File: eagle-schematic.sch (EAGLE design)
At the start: 30 parts, among them IC1 74HC595N, IC2 74HC595N, IC3 74HC595N, IC4 74HC595N, J1 DCJ0202, M1 DC-DC_5-15V_TO_5V

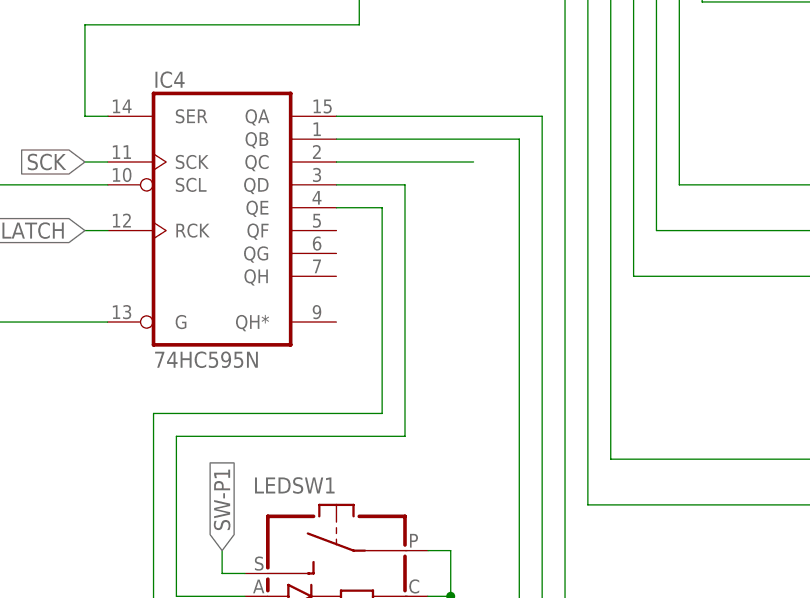
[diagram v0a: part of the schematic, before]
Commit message: Changed wrong connection in schematic
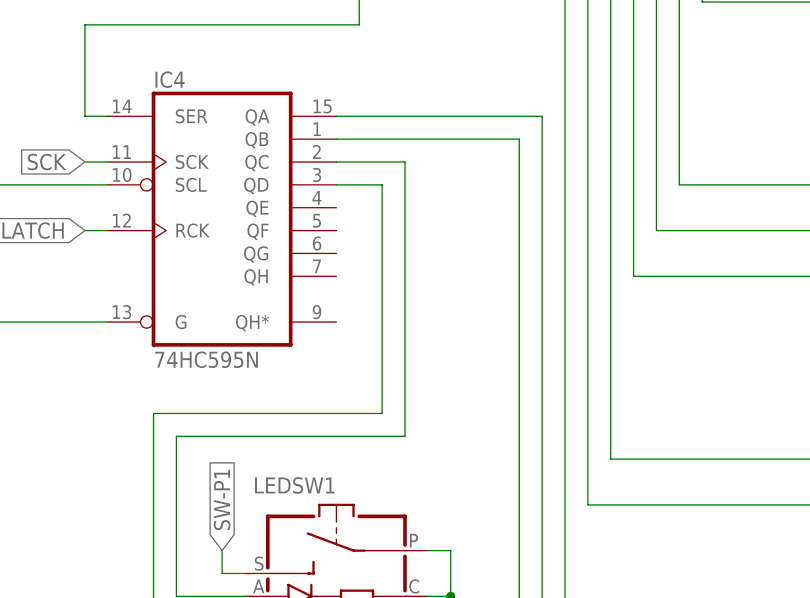
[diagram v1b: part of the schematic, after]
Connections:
- removed net N$39: IC4A.QC
- net N$40: now also IC4A.QC; no longer IC4A.QD
- net N$41: now also IC4A.QD; no longer IC4A.QE
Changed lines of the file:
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@@
-</segment>
-</net>
-<net name="N$39" class="0">
-<segment>
-<pinref part="IC4" gate="A" pin="QC"/>
-<wire x1="210.82" y1="35.56" x2="226.06" y2="35.56" width="0.1524" layer="91"/>
 </segment>
 </net>
@@
 <wire x1="193.04" y1="-12.7" x2="193.04" y2="5.08" width="0.1524" layer="91"/>
 <wire x1="193.04" y1="5.08" x2="218.44" y2="5.08" width="0.1524" layer="91"/>
-<pinref part="IC4" gate="A" pin="QD"/>
-<wire x1="218.44" y1="5.08" x2="218.44" y2="33.02" width="0.1524" layer="91"/>
-<wire x1="218.44" y1="33.02" x2="210.82" y2="33.02" width="0.1524" layer="91"/>
+<wire x1="218.44" y1="5.08" x2="218.44" y2="35.56" width="0.1524" layer="91"/>
 <pinref part="LEDSW1" gate="G$1" pin="A"/>
 <wire x1="200.66" y1="-12.7" x2="193.04" y2="-12.7" width="0.1524" layer="91"/>
+<pinref part="IC4" gate="A" pin="QC"/>
+<wire x1="210.82" y1="35.56" x2="218.44" y2="35.56" width="0.1524" layer="91"/>
 </segment>
 </net>
 <net name="N$41" class="0">
 <segment>
-<pinref part="IC4" gate="A" pin="QE"/>
-<wire x1="210.82" y1="30.48" x2="215.9" y2="30.48" width="0.1524" layer="91"/>
-<wire x1="215.9" y1="30.48" x2="215.9" y2="7.62" width="0.1524" layer="91"/>
+<wire x1="215.9" y1="33.02" x2="215.9" y2="7.62" width="0.1524" layer="91"/>
 <wire x1="215.9" y1="7.62" x2="190.5" y2="7.62" width="0.1524" layer="91"/>
 <wire x1="190.5" y1="7.62" x2="190.5" y2="-40.64" width="0.1524" layer="91"/>
 <pinref part="LEDSW2" gate="G$1" pin="A"/>
 <wire x1="200.66" y1="-40.64" x2="190.5" y2="-40.64" width="0.1524" layer="91"/>
+<pinref part="IC4" gate="A" pin="QD"/>
+<wire x1="210.82" y1="33.02" x2="215.9" y2="33.02" width="0.1524" layer="91"/>
 </segment>
 </net>

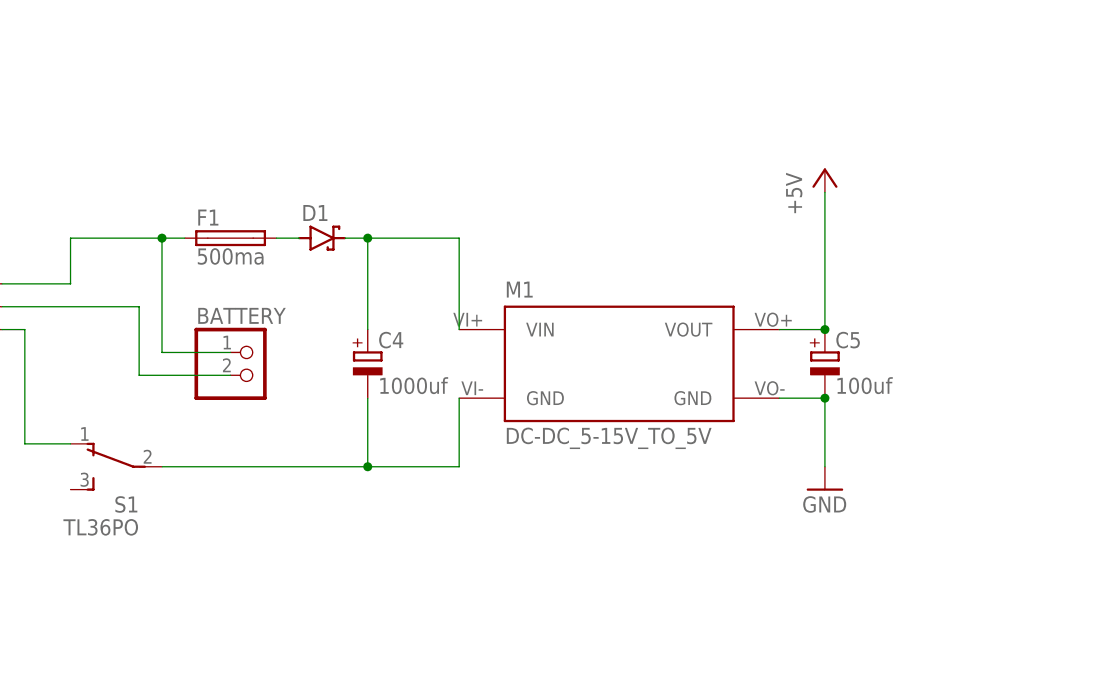
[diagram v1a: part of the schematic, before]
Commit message: Added missing diode value
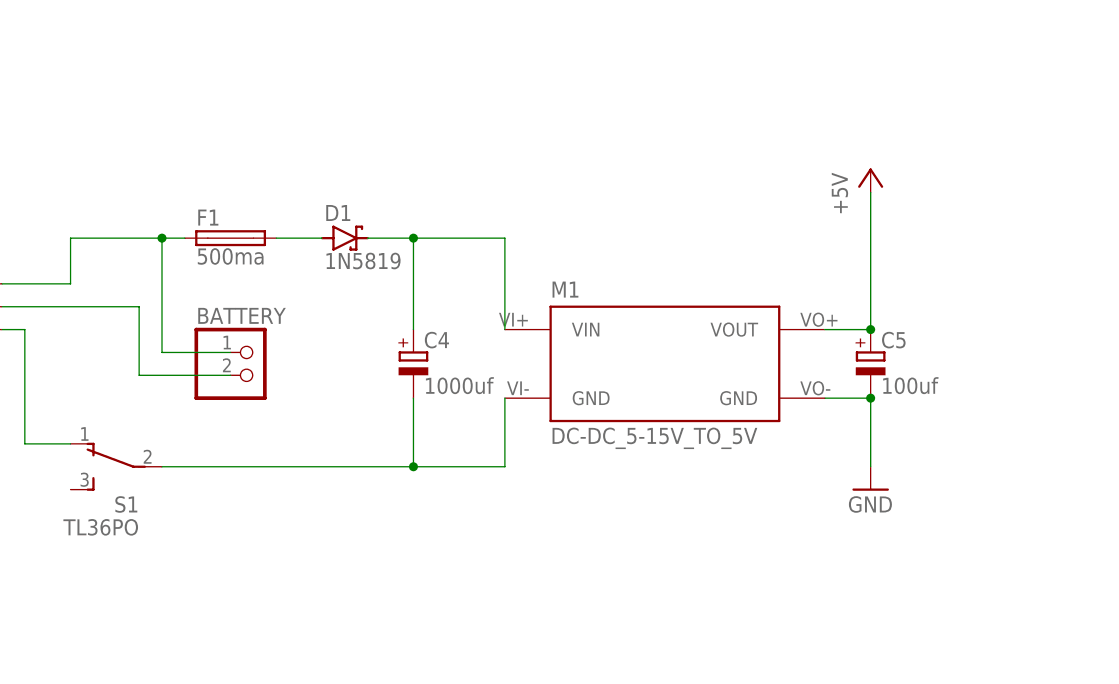
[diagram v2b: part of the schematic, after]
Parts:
- D1: value (none) -> 1N5819
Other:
- moved on the sheet: C4, C5, D1, M1
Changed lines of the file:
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@@
 <part name="F1" library="fuse" library_urn="urn:adsk.eagle:library:233" deviceset="FUSE" device="BLANK_5X20MM" package3d_urn="urn:adsk.eagle:package:14079/1" value="500ma"/>
 <part name="P+1" library="supply1" library_urn="urn:adsk.eagle:library:371" deviceset="+5V" device=""/>
-<part name="D1" library="diode" library_urn="urn:adsk.eagle:library:210" deviceset="SCHOTTKY-DIODE" device="CB417-15" package3d_urn="urn:adsk.eagle:package:43349/2"/>
+<part name="D1" library="diode" library_urn="urn:adsk.eagle:library:210" deviceset="SCHOTTKY-DIODE" device="CB417-15" package3d_urn="urn:adsk.eagle:package:43349/2" value="1N5819"/>
 <part name="R1" library="pot" library_urn="urn:adsk.eagle:library:331" deviceset="TRIM_EU-" device="CIP20C-4MM" package3d_urn="urn:adsk.eagle:package:22718/1" value="10K"/>
 <part name="GND3" library="supply1" library_urn="urn:adsk.eagle:library:371" deviceset="GND" device=""/>
@@
 <attribute name="VALUE" x="116.84" y="81.28" size="1.778" layer="96" rot="R90"/>
 </instance>
-<instance part="D1" gate="G$1" x="66.04" y="144.78" smashed="yes">
-<attribute name="NAME" x="63.754" y="146.685" size="1.778" layer="95"/>
-<attribute name="VALUE" x="63.754" y="141.351" size="1.778" layer="96"/>
+<instance part="D1" gate="G$1" x="68.58" y="144.78" smashed="yes">
+<attribute name="NAME" x="66.294" y="146.685" size="1.778" layer="95"/>
+<attribute name="VALUE" x="66.294" y="141.351" size="1.778" layer="96"/>
 </instance>
 <instance part="R1" gate="1" x="127" y="66.04" smashed="yes" rot="MR0">
@@
 <attribute name="VALUE" x="134.62" y="53.34" size="1.778" layer="96"/>
 </instance>
-<instance part="C4" gate="G$1" x="71.12" y="132.08" smashed="yes">
-<attribute name="NAME" x="72.263" y="132.5626" size="1.778" layer="95"/>
-<attribute name="VALUE" x="72.263" y="127.4826" size="1.778" layer="96"/>
-</instance>
-<instance part="C5" gate="G$1" x="121.92" y="132.08" smashed="yes">
-<attribute name="NAME" x="123.063" y="132.5626" size="1.778" layer="95"/>
-<attribute name="VALUE" x="123.063" y="127.4826" size="1.778" layer="96"/>
-</instance>
-<instance part="M1" gate="G$1" x="99.06" y="132.08" smashed="yes">
-<attribute name="NAME" x="86.36" y="138.176" size="1.778" layer="95"/>
-<attribute name="VALUE" x="86.36" y="121.92" size="1.778" layer="96"/>
-</instance>
-<instance part="P+3" gate="1" x="121.92" y="152.4" smashed="yes">
-<attribute name="VALUE" x="119.38" y="147.32" size="1.778" layer="96" rot="R90"/>
-</instance>
-<instance part="GND2" gate="1" x="121.92" y="116.84" smashed="yes">
-<attribute name="VALUE" x="119.38" y="114.3" size="1.778" layer="96"/>
+<instance part="C4" gate="G$1" x="76.2" y="132.08" smashed="yes">
+<attribute name="NAME" x="77.343" y="132.5626" size="1.778" layer="95"/>
+<attribute name="VALUE" x="77.343" y="127.4826" size="1.778" layer="96"/>
+</instance>
+<instance part="C5" gate="G$1" x="127" y="132.08" smashed="yes">
+<attribute name="NAME" x="128.143" y="132.5626" size="1.778" layer="95"/>
+<attribute name="VALUE" x="128.143" y="127.4826" size="1.778" layer="96"/>
+</instance>
+<instance part="M1" gate="G$1" x="104.14" y="132.08" smashed="yes">
+<attribute name="NAME" x="91.44" y="138.176" size="1.778" layer="95"/>
+<attribute name="VALUE" x="91.44" y="121.92" size="1.778" layer="96"/>
+</instance>
+<instance part="P+3" gate="1" x="127" y="152.4" smashed="yes">
+<attribute name="VALUE" x="124.46" y="147.32" size="1.778" layer="96" rot="R90"/>
+</instance>
+<instance part="GND2" gate="1" x="127" y="116.84" smashed="yes">
+<attribute name="VALUE" x="124.46" y="114.3" size="1.778" layer="96"/>
 </instance>
 <instance part="BATTERY" gate="G$1" x="58.42" y="129.54" smashed="yes">
@@
 <pinref part="M1" gate="G$1" pin="GND@2"/>
 <pinref part="C5" gate="G$1" pin="-"/>
-<wire x1="116.84" y1="127" x2="121.92" y2="127" width="0.1524" layer="91"/>
+<wire x1="121.92" y1="127" x2="127" y2="127" width="0.1524" layer="91"/>
 <pinref part="GND2" gate="1" pin="GND"/>
-<wire x1="121.92" y1="119.38" x2="121.92" y2="127" width="0.1524" layer="91"/>
-<junction x="121.92" y="127"/>
+<wire x1="127" y1="119.38" x2="127" y2="127" width="0.1524" layer="91"/>
+<junction x="127" y="127"/>
 </segment>
 <segment>
@@
 <pinref part="M1" gate="G$1" pin="VOUT"/>
 <pinref part="C5" gate="G$1" pin="+"/>
-<wire x1="116.84" y1="134.62" x2="121.92" y2="134.62" width="0.1524" layer="91"/>
+<wire x1="121.92" y1="134.62" x2="127" y2="134.62" width="0.1524" layer="91"/>
 <pinref part="P+3" gate="1" pin="+5V"/>
-<wire x1="121.92" y1="149.86" x2="121.92" y2="134.62" width="0.1524" layer="91"/>
-<junction x="121.92" y="134.62"/>
+<wire x1="127" y1="149.86" x2="127" y2="134.62" width="0.1524" layer="91"/>
+<junction x="127" y="134.62"/>
 </segment>
 <segment>
@@
 <pinref part="D1" gate="G$1" pin="A"/>
 <pinref part="F1" gate="G$1" pin="2"/>
-<wire x1="63.5" y1="144.78" x2="60.96" y2="144.78" width="0.1524" layer="91"/>
+<wire x1="66.04" y1="144.78" x2="60.96" y2="144.78" width="0.1524" layer="91"/>
 </segment>
 </net>
@@
 <pinref part="D1" gate="G$1" pin="C"/>
 <pinref part="C4" gate="G$1" pin="+"/>
-<wire x1="68.58" y1="144.78" x2="71.12" y2="144.78" width="0.1524" layer="91"/>
-<wire x1="71.12" y1="144.78" x2="71.12" y2="134.62" width="0.1524" layer="91"/>
+<wire x1="71.12" y1="144.78" x2="76.2" y2="144.78" width="0.1524" layer="91"/>
+<wire x1="76.2" y1="144.78" x2="76.2" y2="134.62" width="0.1524" layer="91"/>
 <pinref part="M1" gate="G$1" pin="VIN"/>
-<wire x1="81.28" y1="134.62" x2="81.28" y2="144.78" width="0.1524" layer="91"/>
-<wire x1="81.28" y1="144.78" x2="71.12" y2="144.78" width="0.1524" layer="91"/>
-<junction x="71.12" y="144.78"/>
+<wire x1="86.36" y1="134.62" x2="86.36" y2="144.78" width="0.1524" layer="91"/>
+<wire x1="86.36" y1="144.78" x2="76.2" y2="144.78" width="0.1524" layer="91"/>
+<junction x="76.2" y="144.78"/>
 </segment>
 </net>
@@
 <pinref part="S1" gate="BEF1" pin="P"/>
 <pinref part="C4" gate="G$1" pin="-"/>
-<wire x1="71.12" y1="127" x2="71.12" y2="119.38" width="0.1524" layer="91"/>
-<wire x1="71.12" y1="119.38" x2="48.26" y2="119.38" width="0.1524" layer="91"/>
+<wire x1="76.2" y1="127" x2="76.2" y2="119.38" width="0.1524" layer="91"/>
+<wire x1="76.2" y1="119.38" x2="48.26" y2="119.38" width="0.1524" layer="91"/>
 <pinref part="M1" gate="G$1" pin="GND@1"/>
-<wire x1="81.28" y1="127" x2="81.28" y2="119.38" width="0.1524" layer="91"/>
-<wire x1="81.28" y1="119.38" x2="71.12" y2="119.38" width="0.1524" layer="91"/>
-<junction x="71.12" y="119.38"/>
-</segment>
-</net>
+<wire x1="86.36" y1="127" x2="86.36" y2="119.38" width="0.1524" layer="91"/>
+<wire x1="86.36" y1="119.38" x2="76.2" y2="119.38" width="0.1524" layer="91"/>
+<junction x="76.2" y="119.38"/>
+</segment>
+</net>

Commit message: Updated packages
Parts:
- LEDSW1, LEDSW2: value MCLED -> MC1PLED; device switches-custom:MCLED -> switches-custom:MC1PLED
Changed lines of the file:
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@@
 <part name="P+6" library="supply1" library_urn="urn:adsk.eagle:library:371" deviceset="+5V" device=""/>
 <part name="GND7" library="supply1" library_urn="urn:adsk.eagle:library:371" deviceset="GND" device=""/>
-<part name="RGBSW1" library="switches-custom" deviceset="MC3PRGB" device=""/>
-<part name="RGBSW2" library="switches-custom" deviceset="MC3PRGB" device=""/>
-<part name="RGBSW3" library="switches-custom" deviceset="MC3PRGB" device=""/>
-<part name="RGBSW4" library="switches-custom" deviceset="MC3PRGB" device=""/>
-<part name="RGBSW5" library="switches-custom" deviceset="MC3PRGB" device=""/>
-<part name="RGBSW6" library="switches-custom" deviceset="MC3PRGB" device=""/>
-<part name="RGBSW7" library="switches-custom" deviceset="MC3PRGB" device=""/>
-<part name="RGBSW8" library="switches-custom" deviceset="MC3PRGB" device=""/>
-<part name="RGBSW9" library="switches-custom" deviceset="MC3PRGB" device=""/>
-<part name="LEDSW1" library="switches-custom" library_urn="urn:adsk.eagle:library:37171722" deviceset="MCLED" device="" package3d_urn="urn:adsk.eagle:package:37173483/1"/>
-<part name="LEDSW2" library="switches-custom" library_urn="urn:adsk.eagle:library:37171722" deviceset="MCLED" device="" package3d_urn="urn:adsk.eagle:package:37173483/1"/>
+<part name="RGBSW1" library="switches-custom" library_urn="urn:adsk.eagle:library:37171722" deviceset="MC3PRGB" device="" package3d_urn="urn:adsk.eagle:package:37173484/1"/>
+<part name="RGBSW2" library="switches-custom" library_urn="urn:adsk.eagle:library:37171722" deviceset="MC3PRGB" device="" package3d_urn="urn:adsk.eagle:package:37173484/1"/>
+<part name="RGBSW3" library="switches-custom" library_urn="urn:adsk.eagle:library:37171722" deviceset="MC3PRGB" device="" package3d_urn="urn:adsk.eagle:package:37173484/1"/>
+<part name="RGBSW4" library="switches-custom" library_urn="urn:adsk.eagle:library:37171722" deviceset="MC3PRGB" device="" package3d_urn="urn:adsk.eagle:package:37173484/1"/>
+<part name="RGBSW5" library="switches-custom" library_urn="urn:adsk.eagle:library:37171722" deviceset="MC3PRGB" device="" package3d_urn="urn:adsk.eagle:package:37173484/1"/>
+<part name="RGBSW6" library="switches-custom" library_urn="urn:adsk.eagle:library:37171722" deviceset="MC3PRGB" device="" package3d_urn="urn:adsk.eagle:package:37173484/1"/>
+<part name="RGBSW7" library="switches-custom" library_urn="urn:adsk.eagle:library:37171722" deviceset="MC3PRGB" device="" package3d_urn="urn:adsk.eagle:package:37173484/1"/>
+<part name="RGBSW8" library="switches-custom" library_urn="urn:adsk.eagle:library:37171722" deviceset="MC3PRGB" device="" package3d_urn="urn:adsk.eagle:package:37173484/1"/>
+<part name="RGBSW9" library="switches-custom" library_urn="urn:adsk.eagle:library:37171722" deviceset="MC3PRGB" device="" package3d_urn="urn:adsk.eagle:package:37173484/1"/>
 <part name="GND8" library="supply1" library_urn="urn:adsk.eagle:library:371" deviceset="GND" device=""/>
+<part name="LEDSW1" library="switches-custom" library_urn="urn:adsk.eagle:library:37171722" deviceset="MC1PLED" device="" package3d_urn="urn:adsk.eagle:package:37173483/1"/>
+<part name="LEDSW2" library="switches-custom" library_urn="urn:adsk.eagle:library:37171722" deviceset="MC1PLED" device="" package3d_urn="urn:adsk.eagle:package:37173483/1"/>
 </parts>
 <sheets>
@@
 <attribute name="VALUE" x="294.64" y="-43.18" size="1.778" layer="96" rot="MR0"/>
 </instance>
+<instance part="GND8" gate="1" x="266.7" y="-48.26" smashed="yes">
+<attribute name="VALUE" x="264.16" y="-50.8" size="1.778" layer="96"/>
+</instance>
 <instance part="LEDSW1" gate="G$1" x="210.82" y="-7.62" smashed="yes" rot="MR270">
 <attribute name="NAME" x="210.82" y="-1.27" size="1.778" layer="95" rot="MR0"/>
@@
 <attribute name="NAME" x="210.82" y="-29.21" size="1.778" layer="95" rot="MR0"/>
 <attribute name="VALUE" x="215.9" y="-48.26" size="1.778" layer="96" rot="MR0"/>
-</instance>
-<instance part="GND8" gate="1" x="266.7" y="-48.26" smashed="yes">
-<attribute name="VALUE" x="264.16" y="-50.8" size="1.778" layer="96"/>
 </instance>
 </instances>
@@
 <pinref part="GND8" gate="1" pin="GND"/>
 <junction x="266.7" y="-45.72"/>
-<pinref part="LEDSW1" gate="G$1" pin="P"/>
 <wire x1="220.98" y1="-7.62" x2="223.52" y2="-7.62" width="0.1524" layer="91"/>
-<pinref part="LEDSW1" gate="G$1" pin="C"/>
 <wire x1="220.98" y1="-12.7" x2="223.52" y2="-12.7" width="0.1524" layer="91"/>
 <junction x="223.52" y="-12.7"/>
-<pinref part="LEDSW2" gate="G$1" pin="P"/>
 <wire x1="220.98" y1="-35.56" x2="223.52" y2="-35.56" width="0.1524" layer="91"/>
 <junction x="223.52" y="-35.56"/>
-<pinref part="LEDSW2" gate="G$1" pin="C"/>
 <wire x1="220.98" y1="-40.64" x2="223.52" y2="-40.64" width="0.1524" layer="91"/>
 <junction x="223.52" y="-40.64"/>
+<pinref part="LEDSW1" gate="G$1" pin="P"/>
+<pinref part="LEDSW1" gate="G$1" pin="C"/>
+<pinref part="LEDSW2" gate="G$1" pin="P"/>
+<pinref part="LEDSW2" gate="G$1" pin="C"/>
 </segment>
 </net>
@@
 <wire x1="193.04" y1="5.08" x2="218.44" y2="5.08" width="0.1524" layer="91"/>
 <wire x1="218.44" y1="5.08" x2="218.44" y2="35.56" width="0.1524" layer="91"/>
-<pinref part="LEDSW1" gate="G$1" pin="A"/>
 <wire x1="200.66" y1="-12.7" x2="193.04" y2="-12.7" width="0.1524" layer="91"/>
 <pinref part="IC4" gate="A" pin="QC"/>
 <wire x1="210.82" y1="35.56" x2="218.44" y2="35.56" width="0.1524" layer="91"/>
+<pinref part="LEDSW1" gate="G$1" pin="A"/>
 </segment>
 </net>
@@
 <wire x1="215.9" y1="7.62" x2="190.5" y2="7.62" width="0.1524" layer="91"/>
 <wire x1="190.5" y1="7.62" x2="190.5" y2="-40.64" width="0.1524" layer="91"/>
-<pinref part="LEDSW2" gate="G$1" pin="A"/>
 <wire x1="200.66" y1="-40.64" x2="190.5" y2="-40.64" width="0.1524" layer="91"/>
 <pinref part="IC4" gate="A" pin="QD"/>
 <wire x1="210.82" y1="33.02" x2="215.9" y2="33.02" width="0.1524" layer="91"/>
+<pinref part="LEDSW2" gate="G$1" pin="A"/>
 </segment>
 </net>
 <net name="SW-P1" class="0">
 <segment>
-<pinref part="LEDSW1" gate="G$1" pin="S"/>
 <wire x1="200.66" y1="-10.16" x2="198.12" y2="-10.16" width="0.1524" layer="91"/>
 <wire x1="198.12" y1="-10.16" x2="198.12" y2="-7.62" width="0.1524" layer="91"/>
 <label x="198.12" y="-7.62" size="1.778" layer="95" rot="R90" xref="yes"/>
+<pinref part="LEDSW1" gate="G$1" pin="S"/>
 </segment>
 <segment>
@@
 <net name="SW-P2" class="0">
 <segment>
-<pinref part="LEDSW2" gate="G$1" pin="S"/>
 <wire x1="200.66" y1="-38.1" x2="198.12" y2="-38.1" width="0.1524" layer="91"/>
 <wire x1="198.12" y1="-38.1" x2="198.12" y2="-35.56" width="0.1524" layer="91"/>
 <label x="198.12" y="-35.56" size="1.778" layer="95" rot="R90" xref="yes"/>
-</segment>
-<segment>
+<pinref part="LEDSW2" gate="G$1" pin="S"/>
+</segment>
+<segment>
